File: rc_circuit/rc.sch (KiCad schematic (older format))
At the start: 3 parts

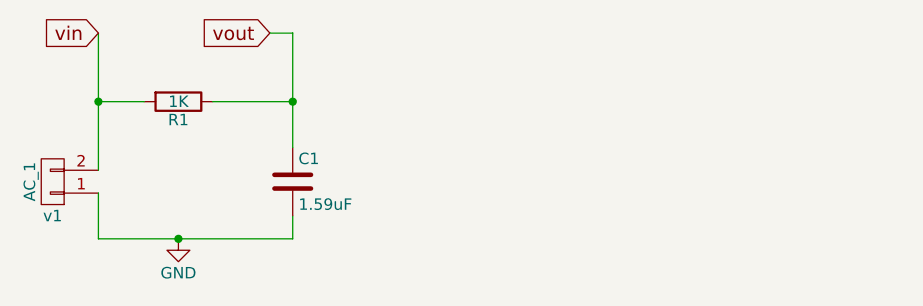
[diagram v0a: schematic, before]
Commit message: Added Simulation Circuits and POV board
Added a BJT characteristics simulation circuit
Add a Voltage Divider simulation circuit
Add an amplifier simulation circuit
Add a Nokia LCD breakout board
Add a POV LED MKL05Z board
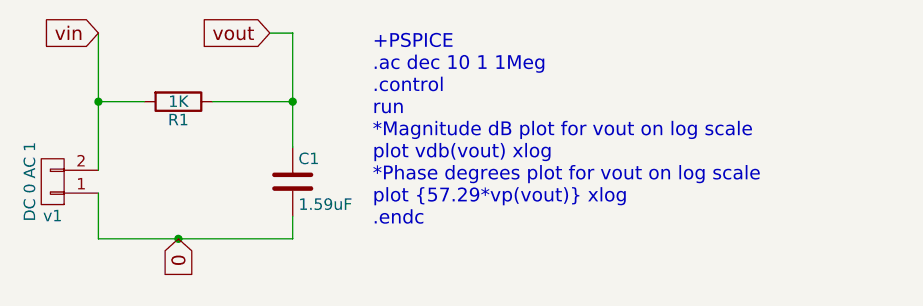
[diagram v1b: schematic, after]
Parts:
- v1: value AC_1 -> DC 0 AC 1
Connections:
- net GND renamed 0
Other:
- note added: "+PSPICE\n.ac dec 10 1 1Meg\n.control\nrun\n*Magnitude dB plot for vout on log scale\nplot vdb(vout) xlog\n*Phase degrees plot for vout on log scale\nplot {57.29*vp(vout)} xlog\n.endc"
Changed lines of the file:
@@
 LIBS:contrib
 LIBS:valves
+LIBS:rc-cache
 EELAYER 25 0
 EELAYER END
@@
 P 2250 3900
 F 0 "v1" H 2250 4050 50  0000 C CNN
-F 1 "AC_1" V 2350 3900 50  0000 C CNN
+F 1 "DC 0 AC 1" V 2350 3900 50  0000 C CNN
 F 2 "" H 2250 3900 50  0000 C CNN
 F 3 "" H 2250 3900 50  0000 C CNN
@@
 	1    0    0    -1
 $EndComp
-$Comp
-L GND #PWR1
-U 1 1 5820806A
-P 2800 4150
-F 0 "#PWR1" H 2800 3900 50  0001 C CNN
-F 1 "GND" H 2800 4000 50  0000 C CNN
-F 2 "" H 2800 4150 50  0000 C CNN
-F 3 "" H 2800 4150 50  0000 C CNN
-	1    2800 4150
-	1    0    0    -1
-$EndComp
 Wire Wire Line
 	2450 3950 2450 4150
@@
 Connection ~ 3300 3550
 Connection ~ 2450 3550
+Text GLabel 2800 4150 3    60   Input ~ 0
+0
+Text Notes 3650 4100 0    60   ~ 0
++PSPICE\n.ac dec 10 1 1Meg\n.control\nrun\n*Magnitude dB plot for vout on log scale\nplot vdb(vout) xlog\n*Phase degrees plot for vout on log scale\nplot {57.29*vp(vout)} xlog\n.endc
 $EndSCHEMATC

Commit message: Too many untracked changes: LCD boards update and switch to KiCAD version 5
Update the Nokia LCD breakout boards
Add more KiCAD simulation projects
Update most projects to KiCAD version 5
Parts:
- C1: symbol C -> rc-rescue:C
- R1: symbol R -> rc-rescue:R
- v1: symbol CONN_01X02 -> rc-rescue:CONN_01X02
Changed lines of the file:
@@
-EESchema Schematic File Version 2
-LIBS:power
-LIBS:device
-LIBS:transistors
-LIBS:conn
-LIBS:linear
-LIBS:regul
-LIBS:74xx
-LIBS:cmos4000
-LIBS:adc-dac
-LIBS:memory
-LIBS:xilinx
-LIBS:microcontrollers
-LIBS:dsp
-LIBS:microchip
-LIBS:analog_switches
-LIBS:motorola
-LIBS:texas
-LIBS:intel
-LIBS:audio
-LIBS:interface
-LIBS:digital-audio
-LIBS:philips
-LIBS:display
-LIBS:cypress
-LIBS:siliconi
-LIBS:opto
-LIBS:atmel
-LIBS:contrib
-LIBS:valves
-LIBS:rc-cache
-EELAYER 25 0
+EESchema Schematic File Version 4
+EELAYER 30 0
 EELAYER END
 $Descr A4 11693 8268
@@
 $EndDescr
 $Comp
-L CONN_01X02 v1
+L rc-rescue:CONN_01X02 v1
 U 1 1 58207F0B
 P 2250 3900
@@
 $EndComp
 $Comp
-L R R1
+L rc-rescue:R R1
 U 1 1 58207F7B
 P 2800 3550
@@
 $EndComp
 $Comp
-L C C1
+L rc-rescue:C C1
 U 1 1 58207FBA
 P 3300 3900
@@
 	2450 3950 2450 4150
 Wire Wire Line
-	2450 4150 3300 4150
-Wire Wire Line
 	3300 4150 3300 4050
-Connection ~ 2800 4150
 Wire Wire Line
 	2650 3550 2450 3550
 Wire Wire Line
-	2450 3250 2450 3850
+	2450 3250 2450 3550
 Wire Wire Line
 	2950 3550 3300 3550
 Wire Wire Line
-	3300 3250 3300 3750
+	3300 3250 3300 3550
 Text GLabel 2450 3250 0    60   Input ~ 0
 vin
@@
 Text Notes 3650 4100 0    60   ~ 0
 +PSPICE\n.ac dec 10 1 1Meg\n.control\nrun\n*Magnitude dB plot for vout on log scale\nplot vdb(vout) xlog\n*Phase degrees plot for vout on log scale\nplot {57.29*vp(vout)} xlog\n.endc
+Wire Wire Line
+	3300 3550 3300 3750
+Wire Wire Line
+	2450 3550 2450 3850
+Wire Wire Line
+	2450 4150 3300 4150
 $EndSCHEMATC
